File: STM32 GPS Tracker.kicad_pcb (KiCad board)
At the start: 4 copper layers, 43.5 x 58.5 mm, 57 parts, among them J1 Screw_Terminal_01x02, J2 LEFT HEADER PINS, J3 693010020611, J4 RIGHT HEADER PINS, Q1 AO3407A, SW1 SW_Push, SW2 SW_Push, U1 SIM808, U2 TPS5430DDA, U3 SMF05CT1G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

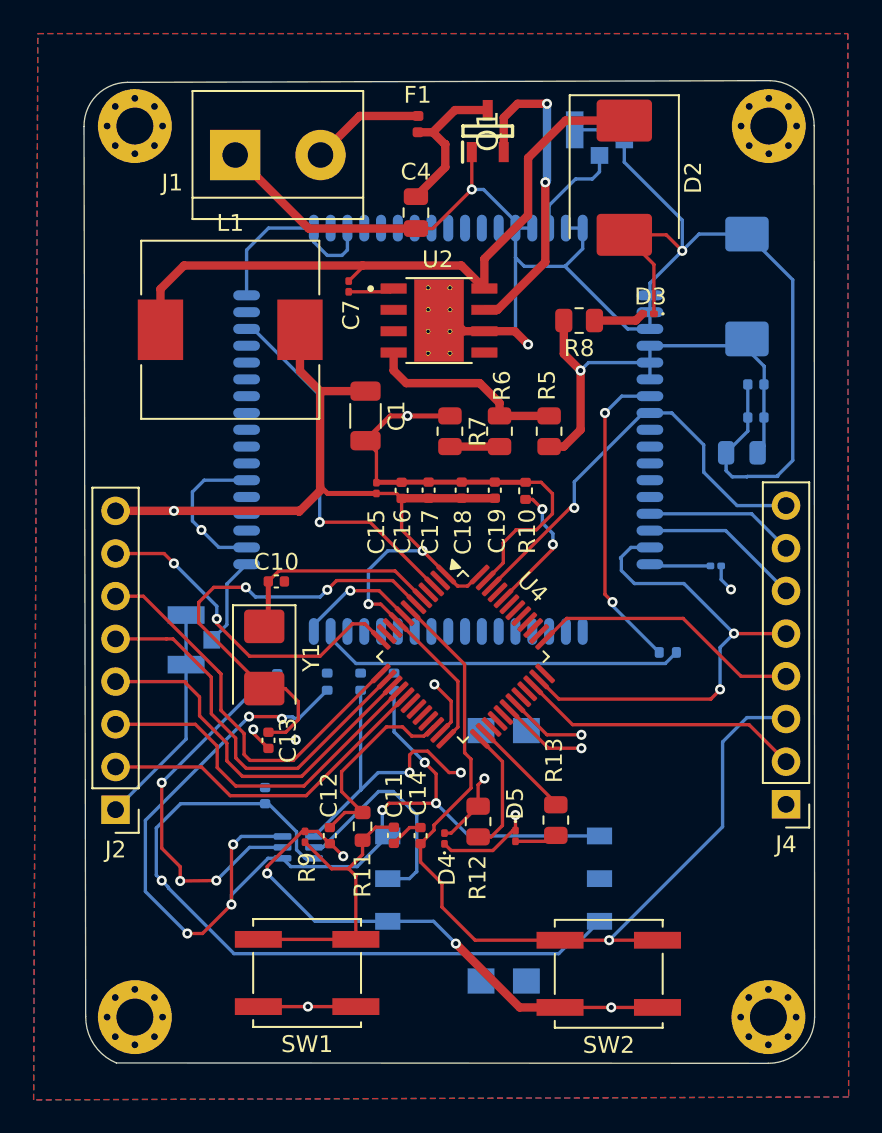
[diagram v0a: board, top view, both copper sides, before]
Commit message: Add STM32F0 GPS tracker firmware (Phase 1-3)
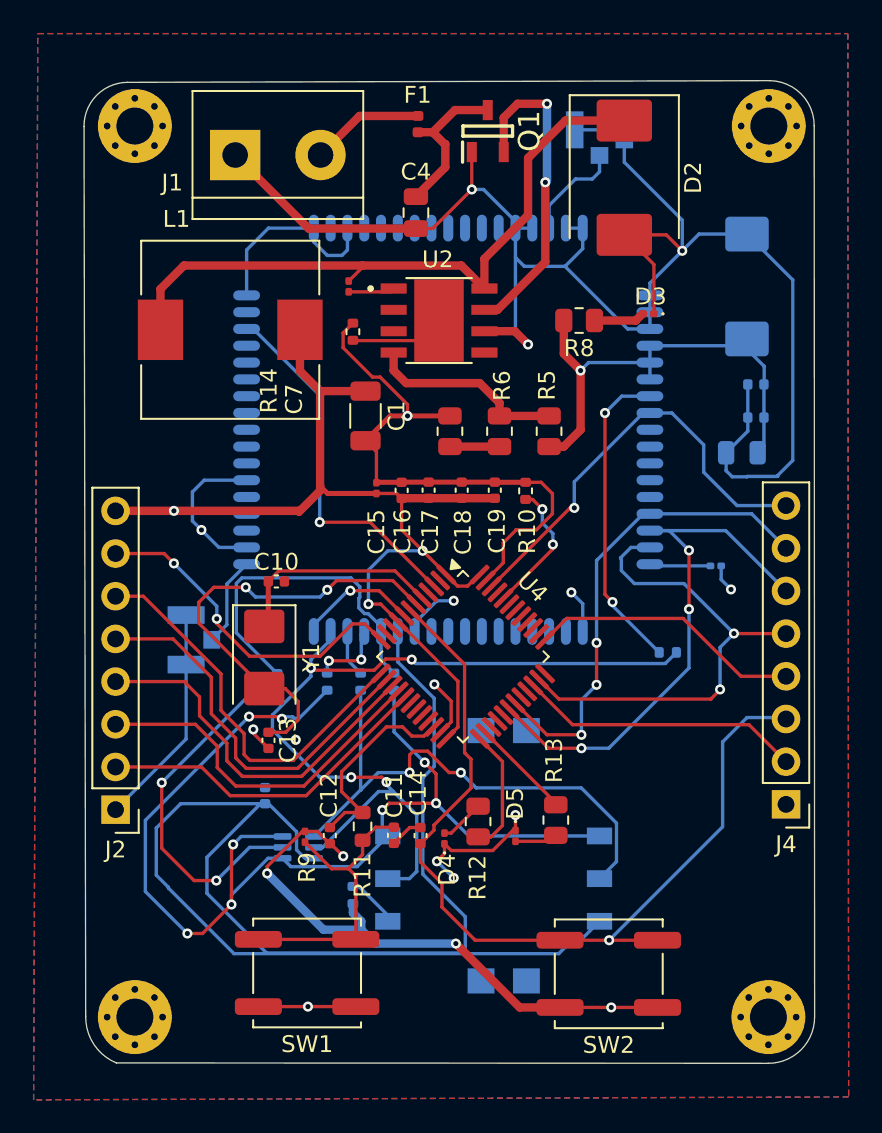
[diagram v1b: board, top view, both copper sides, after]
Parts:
- added R14: 10K, Resistor_SMD:R_0402_1005Metric, F.Cu at (98.5, 80.0)
- added R15: 10K, Resistor_SMD:R_0402_1005Metric, B.Cu at (98.5, 113.5)
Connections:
- J3 pad 5: GND -> Net-(J3-GND)
- U2 pad 9: GND -> Net-(U2-EP)
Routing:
- net SIM_VDD: track 43.9 -> 88.8 mm, vias 1 -> 0
- net SIM_DATA: track 0.00 -> 20.2 mm
- net SIM_RX: track 14.8 -> 33.0 mm, vias 1 -> 3
- net SIM_DET: track 35.2 -> 51.9 mm, vias 0 -> 4
- net SIM_TX: track 13.7 -> 28.7 mm, vias 1 -> 3
- net GND: track 221.9 -> 237.0 mm, vias 14 -> 18
- net Net-(J3-RET): track 17.9 -> 32.1 mm
- net Net-(U2-EP): track 0.00 -> 5.63 mm
- net SIM_CLK: track 0.00 -> 4.48 mm, vias 0 -> 2
- net SIM_RST: track 0.00 -> 2.81 mm
- net Net-(J3-GND): track 0.00 -> 2.78 mm
- net Net-(D4-A): track 4.47 -> 2.66 mm, vias 1 -> 0
- net Net-(C6-Pad2): track 22.4 -> 21.9 mm, vias 3 -> 2
